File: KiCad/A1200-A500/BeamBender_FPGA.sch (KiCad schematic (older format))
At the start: 4 parts, among them U2 GW1NR-UV9LQ144P

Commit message: Added JTAG-pinheader and pull-up resistor arrays
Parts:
- added J6: Conn_02x05_Odd_Even, Connector_PinHeader_2.54mm:PinHeader_2x05_P2.54mm_Vertical_SMD, symbol Connector_Generic:Conn_02x05_Odd_Even
- added RN1, RN2: 10k, BeamBender:RESCAF80P320X160X60-8N, symbol Device:R_Pack04
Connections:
- net labels added: JP1, JP2, JP3
- wire segments 50 -> 56
- no-connect marks 43 -> 41
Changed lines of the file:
@@
 Text GLabel 1600 3400 0    50   Input ~ 0
 GND
-Text GLabel 1600 3700 0    50   Input ~ 0
-GND
+Text GLabel 1600 3300 0    50   Input ~ 0
+JP1
 Text GLabel 1600 4400 0    50   Input ~ 0
 GND
@@
 NoConn ~ 1600 2800
 NoConn ~ 1600 2900
-NoConn ~ 1600 3200
-NoConn ~ 1600 3300
-NoConn ~ 1600 4500
 NoConn ~ 1600 4600
 NoConn ~ 1600 4700
@@
 Text GLabel 4050 650  2    50   Input ~ 0
 GND
-Text GLabel 4050 750  2    50   Input ~ 0
+$Comp
+L Device:R_Pack04 RN1
+U 1 1 6620ABBD
+P 8300 2000
+F 0 "RN1" H 8488 2046 50  0000 L CNN
+F 1 "10k" H 8488 1955 50  0000 L CNN
+F 2 "BeamBender:RESCAF80P320X160X60-8N" V 8575 2000 50  0001 C CNN
+F 3 "~" H 8300 2000 50  0001 C CNN
+	1    8300 2000
+	1    0    0    -1
+$EndComp
+Text GLabel 8400 1800 1    50   Input ~ 0
+3V3
+Wire Wire Line
+	4050 650  4050 750
+Text GLabel 8400 2200 3    50   Input ~ 0
+JP1
+Text GLabel 8200 2200 3    50   Input ~ 0
+TCK
+Text GLabel 8200 1800 1    50   Input ~ 0
 GND
+Text GLabel 8100 2200 3    50   Input ~ 0
+JP2
+Text GLabel 9250 2200 3    50   Input ~ 0
+RECONFIG_N
+Text GLabel 9150 2200 3    50   Input ~ 0
+DONE
+Text GLabel 9050 2200 3    50   Input ~ 0
+READY
+$Comp
+L Device:R_Pack04 RN2
+U 1 1 66213D44
+P 9150 2000
+F 0 "RN2" H 9338 2046 50  0000 L CNN
+F 1 "10k" H 9338 1955 50  0000 L CNN
+F 2 "BeamBender:RESCAF80P320X160X60-8N" V 9425 2000 50  0001 C CNN
+F 3 "~" H 9150 2000 50  0001 C CNN
+	1    9150 2000
+	1    0    0    -1
+$EndComp
+Text GLabel 8950 1800 1    50   Input ~ 0
+3V3
+Wire Wire Line
+	8950 1800 9050 1800
+Connection ~ 9050 1800
+Wire Wire Line
+	9050 1800 9150 1800
+Connection ~ 9150 1800
+Wire Wire Line
+	9150 1800 9250 1800
+Text GLabel 8950 2200 3    50   Input ~ 0
+JP3
+$Comp
+L Connector_Generic:Conn_02x05_Odd_Even J6
+U 1 1 6624BEF7
+P 8200 3550
+F 0 "J6" H 8250 3967 50  0000 C CNN
+F 1 "Conn_02x05_Odd_Even" H 8250 3876 50  0000 C CNN
+F 2 "Connector_PinHeader_2.54mm:PinHeader_2x05_P2.54mm_Vertical_SMD" H 8200 3550 50  0001 C CNN
+F 3 "~" H 8200 3550 50  0001 C CNN
+	1    8200 3550
+	1    0    0    -1
+$EndComp
+Text GLabel 8000 3350 0    50   Output ~ 0
+TCK
+Text GLabel 8000 3450 0    50   Output ~ 0
+TDI
+Text GLabel 8000 3550 0    50   Input ~ 0
+TDO
+Text GLabel 8000 3650 0    50   Input ~ 0
+GND
+Text GLabel 8000 3750 0    50   Output ~ 0
+TMS
+Text GLabel 8500 3350 2    50   Input ~ 0
+GND
+Text GLabel 8500 3750 2    50   Input ~ 0
+GND
+Text GLabel 8500 3550 2    50   Input ~ 0
+3V3
+Text GLabel 1600 3700 0    50   Input ~ 0
+JP2
+Text GLabel 1600 4500 0    50   Input ~ 0
+JP3
+NoConn ~ 1600 3200
+Text GLabel 8500 3650 2    50   Input ~ 0
+JP1
+Text GLabel 8500 3450 2    50   Input ~ 0
+JP2
+Wire Wire Line
+	8200 1800 8300 1800
+Wire Wire Line
+	8200 2200 8300 2200
+Text GLabel 8100 1800 1    50   Input ~ 0
+3V3
 $EndSCHEMATC

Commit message: Fixed JTAG-connector and remaining 3V3-power routing and pull-ups for FPGA
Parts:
- removed J6: Conn_02x05_Odd_Even, Connector_PinHeader_2.54mm:PinHeader_2x05_P2.54mm_Vertical_SMD, symbol Connector_Generic:Conn_02x05_Odd_Even
- added J6: Conn_02x06_Odd_Even, Connector_PinHeader_2.54mm:PinHeader_2x06_P2.54mm_Horizontal, symbol Connector_Generic:Conn_02x06_Odd_Even
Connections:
- net labels added: BT1
- net labels removed: JP3
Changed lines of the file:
@@
 Text GLabel 1600 3400 0    50   Input ~ 0
 GND
-Text GLabel 1600 3300 0    50   Input ~ 0
+Text GLabel 1600 3700 0    50   Input ~ 0
 JP1
 Text GLabel 1600 4400 0    50   Input ~ 0
@@
 Wire Wire Line
 	4050 650  4050 750
-Text GLabel 8400 2200 3    50   Input ~ 0
+Text GLabel 8100 2200 3    50   Input ~ 0
 JP1
 Text GLabel 8200 2200 3    50   Input ~ 0
@@
 Text GLabel 8200 1800 1    50   Input ~ 0
 GND
-Text GLabel 8100 2200 3    50   Input ~ 0
+Text GLabel 8950 2200 3    50   Input ~ 0
 JP2
 Text GLabel 9250 2200 3    50   Input ~ 0
@@
 Wire Wire Line
 	9150 1800 9250 1800
-Text GLabel 8950 2200 3    50   Input ~ 0
-JP3
-$Comp
-L Connector_Generic:Conn_02x05_Odd_Even J6
-U 1 1 6624BEF7
-P 8200 3550
-F 0 "J6" H 8250 3967 50  0000 C CNN
-F 1 "Conn_02x05_Odd_Even" H 8250 3876 50  0000 C CNN
-F 2 "Connector_PinHeader_2.54mm:PinHeader_2x05_P2.54mm_Vertical_SMD" H 8200 3550 50  0001 C CNN
-F 3 "~" H 8200 3550 50  0001 C CNN
-	1    8200 3550
-	1    0    0    -1
-$EndComp
-Text GLabel 8000 3350 0    50   Output ~ 0
+Text GLabel 8400 2200 3    50   Input ~ 0
+BT1
+Text GLabel 8050 3000 0    50   Output ~ 0
 TCK
-Text GLabel 8000 3450 0    50   Output ~ 0
+Text GLabel 8050 3100 0    50   Output ~ 0
 TDI
-Text GLabel 8000 3550 0    50   Input ~ 0
+Text GLabel 8050 3200 0    50   Input ~ 0
 TDO
-Text GLabel 8000 3650 0    50   Input ~ 0
+Text GLabel 8050 3300 0    50   Input ~ 0
 GND
-Text GLabel 8000 3750 0    50   Output ~ 0
+Text GLabel 8050 3400 0    50   Output ~ 0
 TMS
-Text GLabel 8500 3350 2    50   Input ~ 0
+Text GLabel 8550 3000 2    50   Input ~ 0
 GND
-Text GLabel 8500 3750 2    50   Input ~ 0
+Text GLabel 8550 3400 2    50   Input ~ 0
 GND
-Text GLabel 8500 3550 2    50   Input ~ 0
+Text GLabel 8550 3200 2    50   Input ~ 0
 3V3
-Text GLabel 1600 3700 0    50   Input ~ 0
+Text GLabel 1600 4500 0    50   Input ~ 0
 JP2
-Text GLabel 1600 4500 0    50   Input ~ 0
-JP3
+Text GLabel 1600 3300 0    50   Input ~ 0
+BT1
 NoConn ~ 1600 3200
-Text GLabel 8500 3650 2    50   Input ~ 0
+Text GLabel 8550 3300 2    50   Input ~ 0
 JP1
-Text GLabel 8500 3450 2    50   Input ~ 0
+Text GLabel 8550 3100 2    50   Input ~ 0
 JP2
 Wire Wire Line
@@
 Text GLabel 8100 1800 1    50   Input ~ 0
 3V3
+Text GLabel 8550 3500 2    50   Input ~ 0
+BT1
+Text GLabel 8050 3500 0    50   Input ~ 0
+GND
+$Comp
+L Connector_Generic:Conn_02x06_Odd_Even J6
+U 1 1 663407EE
+P 8250 3200
+F 0 "J6" H 8300 3617 50  0000 C CNN
+F 1 "Conn_02x06_Odd_Even" H 8300 3526 50  0000 C CNN
+F 2 "Connector_PinHeader_2.54mm:PinHeader_2x06_P2.54mm_Horizontal" H 8250 3200 50  0001 C CNN
+F 3 "~" H 8250 3200 50  0001 C CNN
+	1    8250 3200
+	1    0    0    -1
+$EndComp
 $EndSCHEMATC

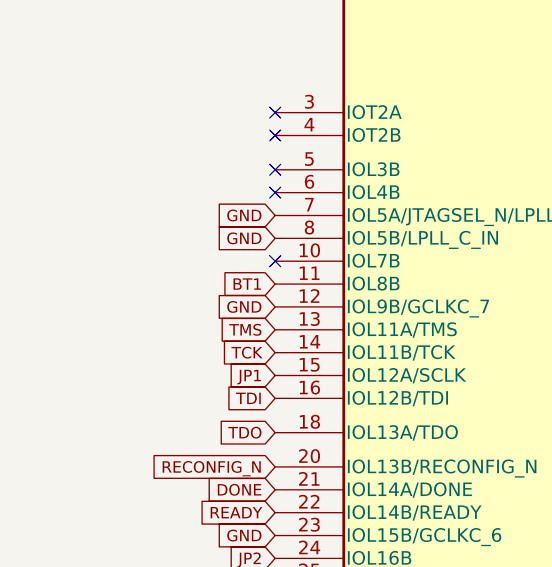
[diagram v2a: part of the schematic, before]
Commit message: Added RC-debounce circuit to Button 1 (BT1)
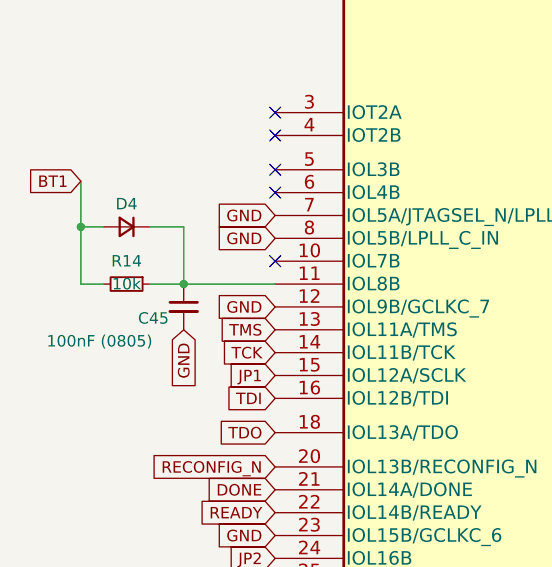
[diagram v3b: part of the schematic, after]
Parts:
- added C45: 100nF (0805), Capacitor_SMD:C_0805_2012Metric_Pad1.18x1.45mm_HandSolder, symbol Device:C_Small
- added D4: D_Small, Diode_SMD:D_0805_2012Metric_Pad1.15x1.40mm_HandSolder, symbol Device:D_Small
- added R14: 10k, Resistor_SMD:R_0805_2012Metric_Pad1.20x1.40mm_HandSolder, symbol Device:R_Small
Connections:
- net BT1: now also D4.2 (A), R14.2; no longer U2.11 (IOL8B)
- net GND: now also C45.2
- new net: C45.1, D4.1 (K), R14.1, U2.11 (IOL8B)
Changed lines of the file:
@@
 Text GLabel 1600 4500 0    50   Input ~ 0
 JP2
-Text GLabel 1600 3300 0    50   Input ~ 0
+Text GLabel 750  2850 0    50   Input ~ 0
 BT1
 NoConn ~ 1600 3200
@@
 	1    0    0    -1
 $EndComp
+$Comp
+L Device:R_Small R14
+U 1 1 6651553B
+P 950 3300
+F 0 "R14" V 850 3300 50  0000 C CNN
+F 1 "10k" V 950 3300 50  0000 C CNN
+F 2 "Resistor_SMD:R_0805_2012Metric_Pad1.20x1.40mm_HandSolder" H 950 3300 50  0001 C CNN
+F 3 "~" H 950 3300 50  0001 C CNN
+	1    950  3300
+	0    1    1    0
+$EndComp
+$Comp
+L Device:C_Small C45
+U 1 1 66517D93
+P 1200 3400
+F 0 "C45" H 1000 3350 50  0000 L CNN
+F 1 "100nF (0805)" H 600 3250 50  0000 L CNN
+F 2 "Capacitor_SMD:C_0805_2012Metric_Pad1.18x1.45mm_HandSolder" H 1200 3400 50  0001 C CNN
+F 3 "~" H 1200 3400 50  0001 C CNN
+	1    1200 3400
+	1    0    0    -1
+$EndComp
+Wire Wire Line
+	1050 3300 1200 3300
+Connection ~ 1200 3300
+Wire Wire Line
+	1200 3300 1600 3300
+Text GLabel 1200 3500 3    50   Input ~ 0
+GND
+Wire Wire Line
+	850  3300 750  3300
+Wire Wire Line
+	750  3300 750  3050
+$Comp
+L Device:D_Small D4
+U 1 1 6651E93A
+P 950 3050
+F 0 "D4" H 950 2950 50  0000 C CNN
+F 1 "D_Small" H 900 2850 50  0001 C CNN
+F 2 "Diode_SMD:D_0805_2012Metric_Pad1.15x1.40mm_HandSolder" V 950 3050 50  0001 C CNN
+F 3 "~" V 950 3050 50  0001 C CNN
+	1    950  3050
+	-1   0    0    1
+$EndComp
+Wire Wire Line
+	750  3050 850  3050
+Connection ~ 750  3050
+Wire Wire Line
+	750  3050 750  2850
+Wire Wire Line
+	1050 3050 1200 3050
+Wire Wire Line
+	1200 3050 1200 3300
 $EndSCHEMATC

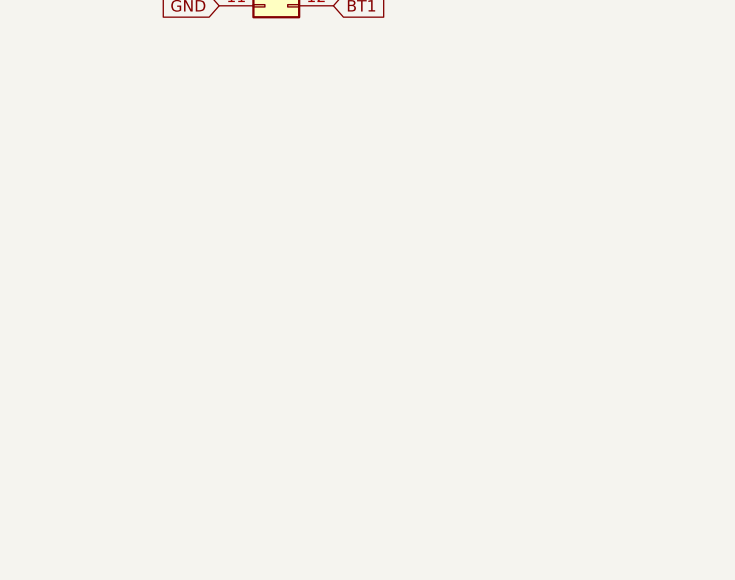
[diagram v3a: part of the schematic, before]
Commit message: Added ADC-chip AK5720VT
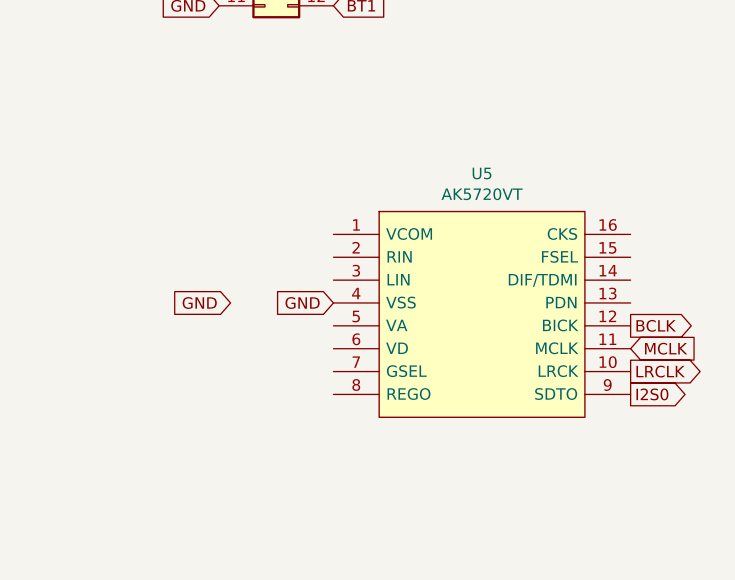
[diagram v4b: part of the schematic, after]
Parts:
- added U5: AK5720VT, Package_SO:TSSOP-16_4.4x5mm_P0.65mm, symbol BeamBender:AK5720VT
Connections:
- net GND: now also U5.4 (VSS)
- new net BCLK: U5.12 (BICK)
- new net I2S0: U5.9 (SDTO)
- new net LRCLK: U5.10 (LRCK)
- new net MCLK: U5.11 (MCLK)
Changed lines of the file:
@@
 Wire Wire Line
 	1200 3050 1200 3300
+$Comp
+L BeamBender:AK5720VT U5
+U 1 1 665688C0
+P 9200 4850
+F 0 "U5" H 9200 5465 50  0000 C CNN
+F 1 "AK5720VT" H 9200 5374 50  0000 C CNN
+F 2 "Package_SO:TSSOP-16_4.4x5mm_P0.65mm" H 10350 4950 50  0001 L CNN
+F 3 "" H 10350 4850 50  0001 L CNN
+F 4 "24-bit Audio ADC" H 10350 4750 50  0001 L CNN "Description"
+	1    9200 4850
+	1    0    0    -1
+$EndComp
+Text GLabel 8100 4800 0    50   Input ~ 0
+GND
+Text GLabel 8550 4800 0    50   Input ~ 0
+GND
+Text GLabel 9850 5200 2    50   Output ~ 0
+I2S0
+Text GLabel 9850 5000 2    50   Input ~ 0
+MCLK
+Text GLabel 9850 5100 2    50   Output ~ 0
+LRCLK
+Text GLabel 9850 4900 2    50   Output ~ 0
+BCLK
 $EndSCHEMATC

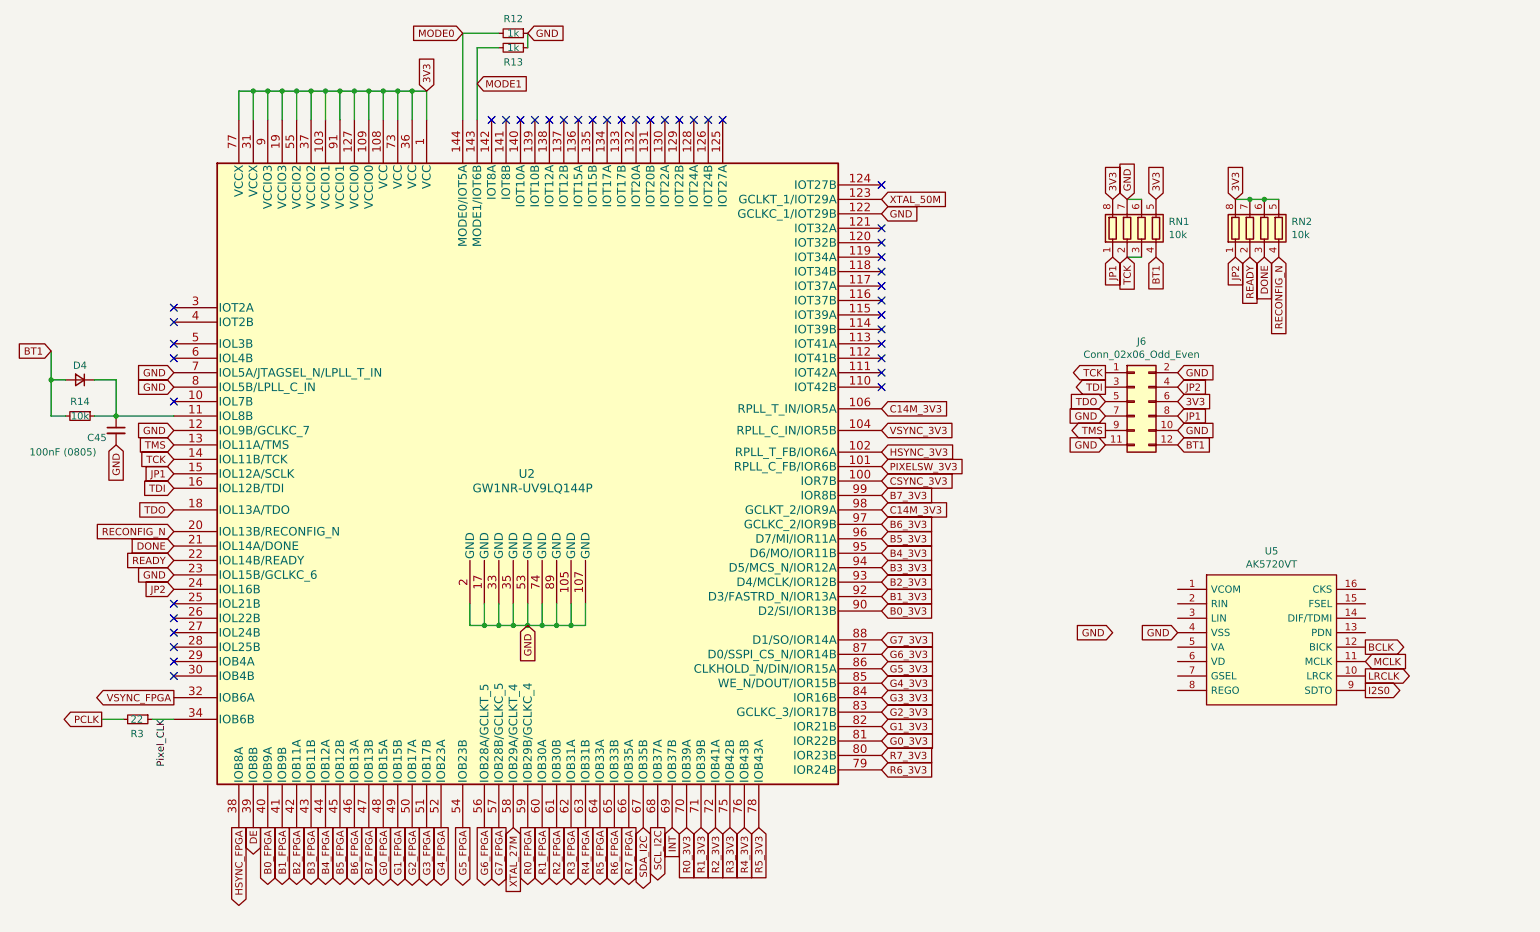
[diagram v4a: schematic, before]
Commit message: added a 24.576 MHz crystal oscillator 5.0x3.2mm for Audio MCLK routed to FPGA pin 98 (GCLKT_2)
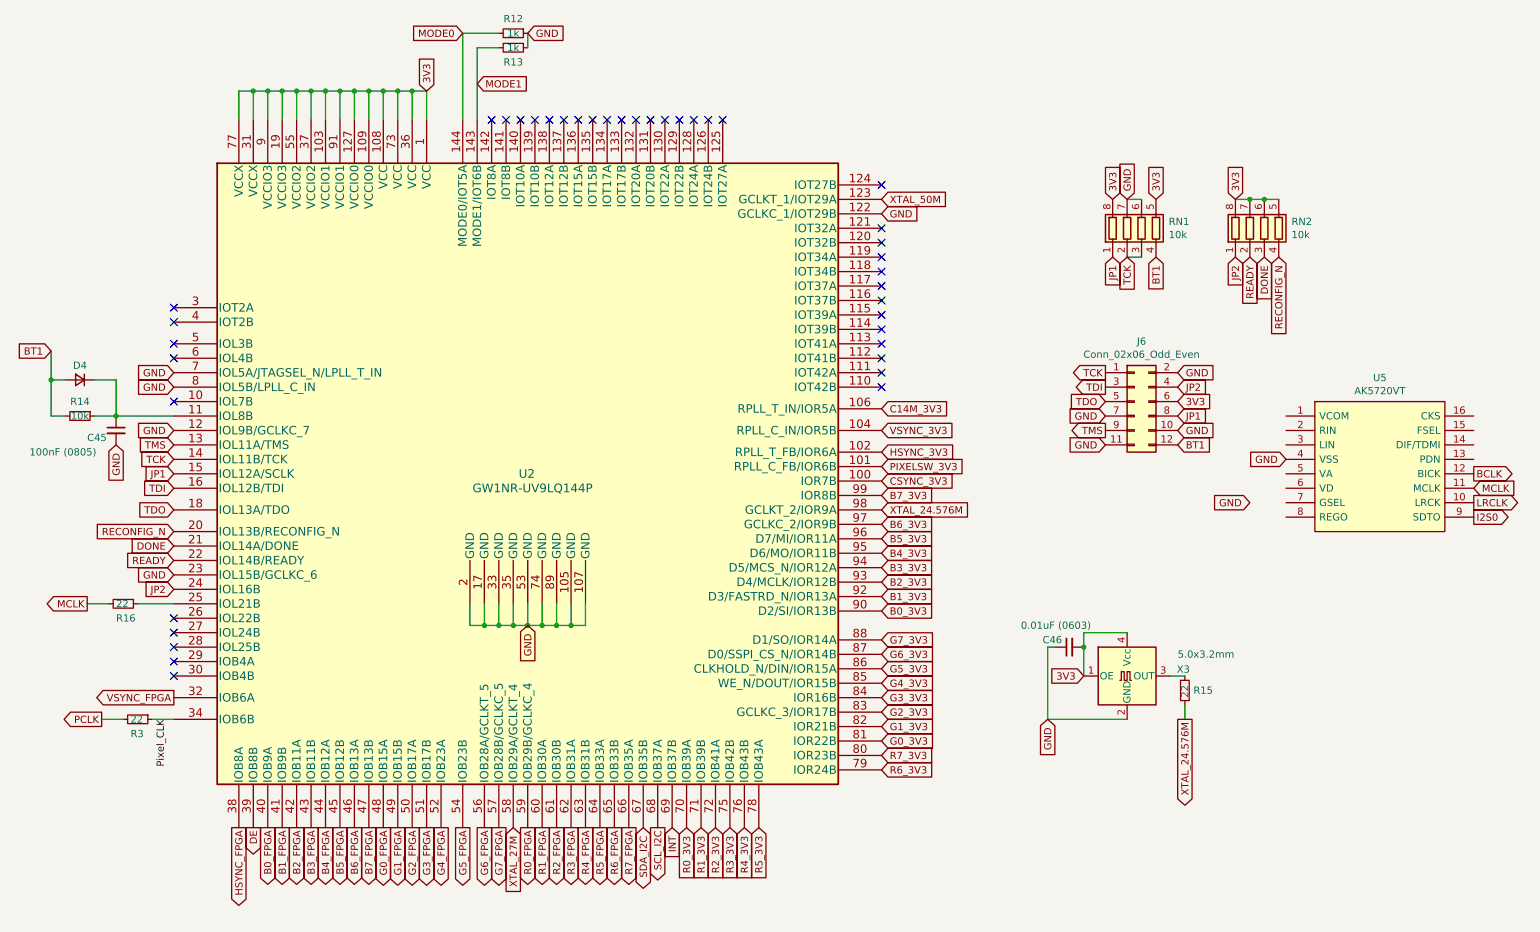
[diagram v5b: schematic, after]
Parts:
- added C46: 0.01uF (0603), Capacitor_SMD:C_0603_1608Metric_Pad1.08x0.95mm_HandSolder, symbol Device:C_Small
- added R15, R16: 22, Resistor_SMD:R_0603_1608Metric_Pad0.98x0.95mm_HandSolder, symbol Device:R_Small
- added X3: 5.0x3.2mm, Oscillator:Oscillator_SMD_TXC_7C-4Pin_5.0x3.2mm_HandSoldering, symbol Oscillator:SG-8002LB
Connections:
- net 3V3: now also C46.2, X3.1 (OE), X3.4 (Vcc)
- net C14M_3V3: no longer U2.98 (GCLKT_2/IOR9A)
- net GND: now also C46.1, X3.2 (GND)
- net MCLK: now also R16.2
- net at U2.25 (IOL21B): now also R16.1
- new net: R15.1, X3.3 (OUT)
- new net XTAL_24.576M: R15.2, U2.98 (GCLKT_2/IOR9A)
- no-connect marks 41 -> 40
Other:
- moved on the sheet: U5
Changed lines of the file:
@@
 Text GLabel 6500 3550 2    50   Input ~ 0
 HSYNC_3V3
-Text GLabel 6500 3950 2    50   Input ~ 0
-C14M_3V3
 Text GLabel 2250 6150 3    50   Output ~ 0
 B0_FPGA
@@
 NoConn ~ 1600 2800
 NoConn ~ 1600 2900
-NoConn ~ 1600 4600
 NoConn ~ 1600 4700
 NoConn ~ 1600 4800
@@
 L BeamBender:AK5720VT U5
 U 1 1 665688C0
-P 9200 4850
-F 0 "U5" H 9200 5465 50  0000 C CNN
-F 1 "AK5720VT" H 9200 5374 50  0000 C CNN
-F 2 "Package_SO:TSSOP-16_4.4x5mm_P0.65mm" H 10350 4950 50  0001 L CNN
-F 3 "" H 10350 4850 50  0001 L CNN
-F 4 "24-bit Audio ADC" H 10350 4750 50  0001 L CNN "Description"
-	1    9200 4850
-	1    0    0    -1
-$EndComp
-Text GLabel 8100 4800 0    50   Input ~ 0
-GND
-Text GLabel 8550 4800 0    50   Input ~ 0
-GND
-Text GLabel 9850 5200 2    50   Output ~ 0
+P 9950 3650
+F 0 "U5" H 9950 4265 50  0000 C CNN
+F 1 "AK5720VT" H 9950 4174 50  0000 C CNN
+F 2 "Package_SO:TSSOP-16_4.4x5mm_P0.65mm" H 11100 3750 50  0001 L CNN
+F 3 "" H 11100 3650 50  0001 L CNN
+F 4 "24-bit Audio ADC" H 11100 3550 50  0001 L CNN "Description"
+	1    9950 3650
+	1    0    0    -1
+$EndComp
+Text GLabel 9050 3900 0    50   Input ~ 0
+GND
+Text GLabel 9300 3600 0    50   Input ~ 0
+GND
+Text GLabel 10600 4000 2    50   Output ~ 0
 I2S0
-Text GLabel 9850 5000 2    50   Input ~ 0
+Text GLabel 10600 3800 2    50   Input ~ 0
 MCLK
-Text GLabel 9850 5100 2    50   Output ~ 0
+Text GLabel 10600 3900 2    50   Output ~ 0
 LRCLK
-Text GLabel 9850 4900 2    50   Output ~ 0
+Text GLabel 10600 3700 2    50   Output ~ 0
 BCLK
+Text GLabel 7900 5100 0    50   Input ~ 0
+3V3
+Wire Wire Line
+	8200 4800 7900 4800
+Wire Wire Line
+	7900 4800 7900 4900
+$Comp
+L Device:R_Small R15
+U 1 1 665DD143
+P 8600 5200
+F 0 "R15" H 8659 5200 50  0000 L CNN
+F 1 "22" V 8600 5150 50  0000 L CNN
+F 2 "Resistor_SMD:R_0603_1608Metric_Pad0.98x0.95mm_HandSolder" H 8600 5200 50  0001 C CNN
+F 3 "~" H 8600 5200 50  0001 C CNN
+	1    8600 5200
+	1    0    0    -1
+$EndComp
+Wire Wire Line
+	8600 5300 8600 5400
+Wire Wire Line
+	8500 5100 8600 5100
+Text GLabel 8600 5400 3    50   Output ~ 0
+XTAL_24.576M
+$Comp
+L Device:C_Small C46
+U 1 1 665DD14C
+P 7800 4900
+F 0 "C46" V 7850 4950 50  0000 L CNN
+F 1 "0.01uF (0603)" V 7950 4750 50  0000 L CNN
+F 2 "Capacitor_SMD:C_0603_1608Metric_Pad1.08x0.95mm_HandSolder" H 7800 4900 50  0001 C CNN
+F 3 "~" H 7800 4900 50  0001 C CNN
+	1    7800 4900
+	0    -1   -1   0
+$EndComp
+Connection ~ 7900 4900
+Wire Wire Line
+	7900 4900 7900 5100
+Text GLabel 7650 5400 3    50   Input ~ 0
+GND
+Wire Wire Line
+	8200 5400 7650 5400
+Wire Wire Line
+	7650 5400 7650 4900
+Wire Wire Line
+	7650 4900 7700 4900
+$Comp
+L Oscillator:SG-8002LB X3
+U 1 1 665EF5A4
+P 8200 5100
+F 0 "X3" H 8544 5146 50  0000 L CNN
+F 1 "5.0x3.2mm" H 8550 5250 50  0000 L CNN
+F 2 "Oscillator:Oscillator_SMD_TXC_7C-4Pin_5.0x3.2mm_HandSoldering" H 8900 4750 50  0001 C CNN
+F 3 "" H 8100 5100 50  0001 C CNN
+	1    8200 5100
+	1    0    0    -1
+$EndComp
+Text GLabel 6500 3950 2    50   Input ~ 0
+XTAL_24.576M
+Text GLabel 1000 4600 0    50   Output ~ 0
+MCLK
+$Comp
+L Device:R_Small R?
+U 1 1 666738D2
+P 1250 4600
+AR Path="/666738D2" Ref="R?"  Part="1"
+AR Path="/6541C824/666738D2" Ref="R16"  Part="1"
+F 0 "R16" V 1350 4550 50  0000 L CNN
+F 1 "22" V 1250 4550 50  0000 L CNN
+F 2 "Resistor_SMD:R_0603_1608Metric_Pad0.98x0.95mm_HandSolder" H 1250 4600 50  0001 C CNN
+F 3 "~" H 1250 4600 50  0001 C CNN
+	1    1250 4600
+	0    1    1    0
+$EndComp
+Wire Wire Line
+	1150 4600 1000 4600
+Wire Wire Line
+	1350 4600 1600 4600
 $EndSCHEMATC
